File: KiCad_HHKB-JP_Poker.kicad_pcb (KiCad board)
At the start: 2 copper layers, 285 x 95.1 mm, 158 parts, among them SW1 SW_Push, U1 ATmega32U4-MU, U2 PRTR5V0U2X, Y1 16MHz

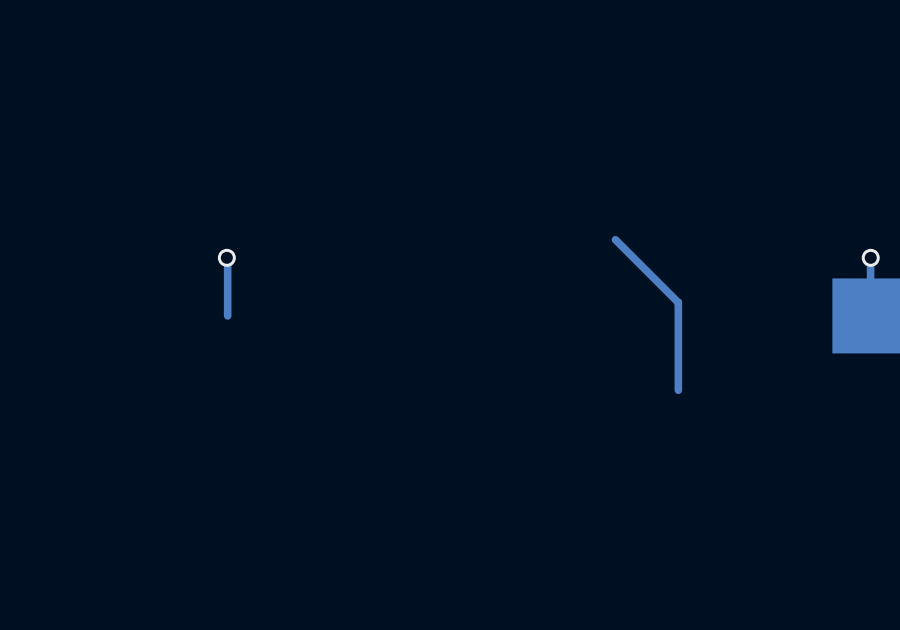
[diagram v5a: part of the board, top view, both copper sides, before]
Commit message: B.Cuの消し残しを削除
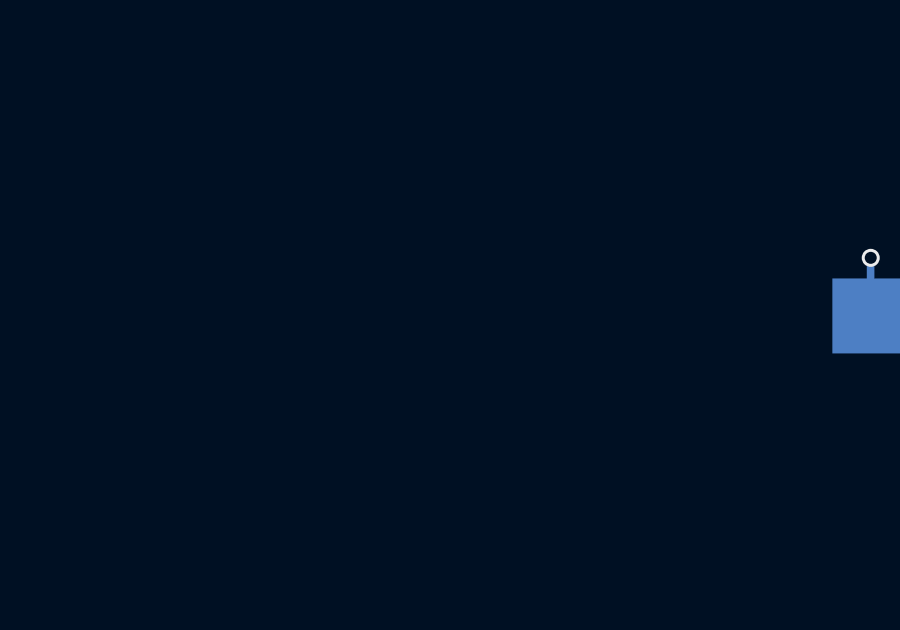
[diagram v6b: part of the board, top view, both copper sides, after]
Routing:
- net Net-(D10-Pad2): track 5.89 -> 0.00 mm
- net COL10: track 67.9 -> 65.9 mm, vias 5 -> 4
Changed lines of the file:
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@@
   (via (at 326.39 200.279) (size 0.6) (drill 0.4) (layers "F.Cu" "B.Cu") (net 79))
   (via (at 341.376 238.379) (size 0.6) (drill 0.4) (layers "F.Cu" "B.Cu") (net 79))
-  (via (at 329.438 253.492) (size 0.6) (drill 0.4) (layers "F.Cu" "B.Cu") (net 79))
   (via (at 331.851 219.329) (size 0.6) (drill 0.4) (layers "F.Cu" "B.Cu") (net 79))
   (segment (start 331.851 219.329) (end 331.851 217.3335) (width 0.254) (layer "B.Cu") (net 79))
   (segment (start 196.6085 311.016) (end 201.80375 311.016) (width 0.254) (layer "B.Cu") (net 79))
   (segment (start 326.39 200.279) (end 326.39 198.9725) (width 0.254) (layer "B.Cu") (net 79))
-  (segment (start 329.438 253.492) (end 329.465 253.519) (width 0.254) (layer "B.Cu") (net 79))
   (segment (start 202.781 307.37175) (end 205.829 304.32375) (width 0.254) (layer "B.Cu") (net 79))
   (segment (start 317.55875 181.17025) (end 317.5 181.229) (width 0.254) (layer "B.Cu") (net 79))
   (segment (start 341.376 236.3835) (end 341.37125 236.37875) (width 0.254) (layer "B.Cu") (net 79))
   (segment (start 201.80375 311.016) (end 202.781 310.03875) (width 0.254) (layer "B.Cu") (net 79))
-  (segment (start 329.465 253.519) (end 329.465 255.42875) (width 0.254) (layer "B.Cu") (net 79))
   (segment (start 317.55875 179.22875) (end 317.55875 181.17025) (width 0.254) (layer "B.Cu") (net 79))
   (segment (start 341.376 238.379) (end 341.376 236.3835) (width 0.254) (layer "B.Cu") (net 79))
@@
   (segment (start 206.375 254.98425) (end 204.2795 252.88875) (width 0.254) (layer "B.Cu") (net 96))
   (segment (start 206.375 257.90625) (end 206.375 254.98425) (width 0.254) (layer "B.Cu") (net 96))
-  (segment (start 344.4875 257.90625) (end 344.4875 254.98425) (width 0.254) (layer "B.Cu") (net 97))
-  (segment (start 344.4875 254.98425) (end 342.392 252.88875) (width 0.254) (layer "B.Cu") (net 97))
   (segment (start 144.653 189.103) (end 141.986 189.103) (width 0.381) (layer "F.Cu") (net 98))
   (segment (start 145.923 181.864) (end 142.24 181.864) (width 0.381) (layer "F.Cu") (net 98))

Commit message: RIGHT の Footprint を 1.25 -> 1U に変更
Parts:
- K_RIGHT1: footprint MX_Only:MXOnly-1.25U-Hotswap -> MX_Only:MXOnly-1U-Hotswap
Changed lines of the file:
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@@
     )
   )
-  (footprint "MX_Only:MXOnly-1.25U-Hotswap" (layer "F.Cu")
+  (footprint "MX_Only:MXOnly-1U-Hotswap" (layer "F.Cu")
     (at 398.4625 257.96875)
     (property "Sheetfile" "matrix.kicad_sch")
     (property "Sheetname" "matrix")
     (attr smd)
-    (fp_text reference "K_RIGHT1" (at 0 3.048) (layer "B.Fab")
+    (fp_text reference "K_RIGHT1" (at 0 3.175) (layer "B.Fab")
       (effects (font (size 1 1) (thickness 0.15)) (justify mirror))
     )
@@
       (effects (font (size 1 1) (thickness 0.15)))
     )
+    (fp_line (start -9.525 9.525) (end -9.525 -9.525) (layer "Dwgs.User") (width 0.15))
+    (fp_line (start 7 -7) (end 7 -5) (layer "Dwgs.User") (width 0.15))
+    (fp_line (start 9.525 -9.525) (end 9.525 9.525) (layer "Dwgs.User") (width 0.15))
     (fp_line (start 7 7) (end 7 5) (layer "Dwgs.User") (width 0.15))
-    (fp_line (start -11.90625 9.525) (end -11.90625 -9.525) (layer "Dwgs.User") (width 0.15))
+    (fp_line (start -7 5) (end -7 7) (layer "Dwgs.User") (width 0.15))
+    (fp_line (start -7 -7) (end -7 -5) (layer "Dwgs.User") (width 0.15))
+    (fp_line (start -5 -7) (end -7 -7) (layer "Dwgs.User") (width 0.15))
+    (fp_line (start 5 7) (end 7 7) (layer "Dwgs.User") (width 0.15))
+    (fp_line (start 9.525 9.525) (end -9.525 9.525) (layer "Dwgs.User") (width 0.15))
+    (fp_line (start -9.525 -9.525) (end 9.525 -9.525) (layer "Dwgs.User") (width 0.15))
+    (fp_line (start 5 -7) (end 7 -7) (layer "Dwgs.User") (width 0.15))
     (fp_line (start -7 7) (end -5 7) (layer "Dwgs.User") (width 0.15))
-    (fp_line (start 5 7) (end 7 7) (layer "Dwgs.User") (width 0.15))
-    (fp_line (start -7 -7) (end -7 -5) (layer "Dwgs.User") (width 0.15))
-    (fp_line (start 11.90625 9.525) (end -11.90625 9.525) (layer "Dwgs.User") (width 0.15))
-    (fp_line (start 7 -7) (end 7 -5) (layer "Dwgs.User") (width 0.15))
-    (fp_line (start -5 -7) (end -7 -7) (layer "Dwgs.User") (width 0.15))
-    (fp_line (start -7 5) (end -7 7) (layer "Dwgs.User") (width 0.15))
-    (fp_line (start -11.90625 -9.525) (end 11.90625 -9.525) (layer "Dwgs.User") (width 0.15))
-    (fp_line (start 5 -7) (end 7 -7) (layer "Dwgs.User") (width 0.15))
-    (fp_line (start 11.90625 -9.525) (end 11.90625 9.525) (layer "Dwgs.User") (width 0.15))
+    (fp_line (start -0.4 -2.6) (end 5.3 -2.6) (layer "B.CrtYd") (width 0.127))
+    (fp_line (start -5.842 -1.27) (end -5.842 -3.81) (layer "B.CrtYd") (width 0.15))
+    (fp_line (start 7.112 -3.81) (end 4.572 -3.81) (layer "B.CrtYd") (width 0.15))
+    (fp_line (start -6.5 -0.6) (end -2.4 -0.6) (layer "B.CrtYd") (width 0.127))
+    (fp_line (start 5.3 -7) (end 5.3 -2.6) (layer "B.CrtYd") (width 0.127))
+    (fp_line (start 4.572 -3.81) (end 4.572 -6.35) (layer "B.CrtYd") (width 0.15))
+    (fp_line (start -6.5 -4.5) (end -6.5 -0.6) (layer "B.CrtYd") (width 0.127))
+    (fp_line (start 5.3 -7) (end -4 -7) (layer "B.CrtYd") (width 0.127))
     (fp_line (start 4.572 -6.35) (end 7.112 -6.35) (layer "B.CrtYd") (width 0.15))
-    (fp_line (start 4.572 -3.81) (end 4.572 -6.35) (layer "B.CrtYd") (width 0.15))
-    (fp_line (start -6.5 -0.6) (end -2.4 -0.6) (layer "B.CrtYd") (width 0.127))
+    (fp_line (start -8.382 -3.81) (end -8.382 -1.27) (layer "B.CrtYd") (width 0.15))
     (fp_line (start 7.112 -6.35) (end 7.112 -3.81) (layer "B.CrtYd") (width 0.15))
-    (fp_line (start 7.112 -3.81) (end 4.572 -3.81) (layer "B.CrtYd") (width 0.15))
-    (fp_line (start 5.3 -7) (end -4 -7) (layer "B.CrtYd") (width 0.127))
-    (fp_line (start -6.5 -4.5) (end -6.5 -0.6) (layer "B.CrtYd") (width 0.127))
-    (fp_line (start 5.3 -7) (end 5.3 -2.6) (layer "B.CrtYd") (width 0.127))
-    (fp_line (start -8.382 -1.27) (end -8.382 -3.81) (layer "B.CrtYd") (width 0.15))
-    (fp_line (start -0.4 -2.6) (end 5.3 -2.6) (layer "B.CrtYd") (width 0.127))
-    (fp_line (start -5.842 -1.27) (end -8.382 -1.27) (layer "B.CrtYd") (width 0.15))
-    (fp_line (start -5.842 -3.81) (end -5.842 -1.27) (layer "B.CrtYd") (width 0.15))
-    (fp_line (start -8.382 -3.81) (end -5.842 -3.81) (layer "B.CrtYd") (width 0.15))
+    (fp_line (start -5.842 -3.81) (end -8.382 -3.81) (layer "B.CrtYd") (width 0.15))
+    (fp_line (start -8.382 -1.27) (end -5.842 -1.27) (layer "B.CrtYd") (width 0.15))
     (fp_arc (start -2.4 -0.6) (mid -1.814214 -2.014214) (end -0.4 -2.6) (layer "B.CrtYd") (width 0.127))
     (fp_arc (start -6.5 -4.5) (mid -5.767767 -6.267767) (end -4 -7) (layer "B.CrtYd") (width 0.127))
+    (fp_circle (center 2.54 -5.08) (end 2.54 -6.604) (layer "B.CrtYd") (width 0.15) (fill none))
     (fp_circle (center -3.81 -2.54) (end -3.81 -4.064) (layer "B.CrtYd") (width 0.15) (fill none))
-    (fp_circle (center 2.54 -5.08) (end 2.54 -6.604) (layer "B.CrtYd") (width 0.15) (fill none))
+    (pad "" np_thru_hole circle locked (at 5.08 0 48.0996) (size 1.75 1.75) (drill 1.75) (layers *.Cu *.Mask))
+    (pad "" np_thru_hole circle locked (at 2.54 -5.08) (size 3 3) (drill 3) (layers *.Cu *.Mask))
+    (pad "" np_thru_hole circle locked (at 0 0) (size 3.9878 3.9878) (drill 3.9878) (layers *.Cu *.Mask))
     (pad "" np_thru_hole circle locked (at -3.81 -2.54) (size 3 3) (drill 3) (layers *.Cu *.Mask))
     (pad "" np_thru_hole circle locked (at -5.08 0 48.0996) (size 1.75 1.75) (drill 1.75) (layers *.Cu *.Mask))
-    (pad "" np_thru_hole circle locked (at 5.08 0 48.0996) (size 1.75 1.75) (drill 1.75) (layers *.Cu *.Mask))
-    (pad "" np_thru_hole circle locked (at 0 0) (size 3.9878 3.9878) (drill 3.9878) (layers *.Cu *.Mask))
-    (pad "" np_thru_hole circle locked (at 2.54 -5.08) (size 3 3) (drill 3) (layers *.Cu *.Mask))
     (pad "1" smd rect locked (at -7.085 -2.54) (size 2.55 2.5) (layers "B.Cu" "B.Paste" "B.Mask")
       (net 82 "COL13") (pinfunction "COL") (pintype "passive"))
@@
     (model "${KILIB}/MX_Alps_Hybrid.pretty/MX_Only.pretty/3d_shapes/CPG151101S11.wrl"
       (offset (xyz 0 0 -1.4868))
-      (scale (xyz 0.3937 0.3937 0.3937))
+      (scale (xyz 0.393701 0.3937 0.393701))
       (rotate (xyz 0 0 0))
     )

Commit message: R4(zxc列)のキースイッチ配置完了
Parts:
- D10, D11, D37, D42, D43: moved to B.Cu
- moved K_UP1 120.7 mm to (381.8, 238.9)
- moved D11 34.3 mm to (324.1, 303.4), turned to 180 degrees
- moved D42 34.3 mm to (324.1, 306.8), turned to 180 degrees
- moved D37 23.4 mm to (318.4, 303.4), turned to 180 degrees
- moved D43 21.0 mm to (331.9, 295.4), turned to 180 degrees
- moved D67 15.6 mm to (393.8, 243.9)
- moved K_RSFT1 7.14 mm to (400.8, 238.9)
- moved D22 4.76 mm to (370.7, 240.5)
- moved D41 4.76 mm to (275.4, 240.5)
- moved K_N1 4.76 mm to (267.5, 238.9)
- moved K_UNSC1 4.76 mm to (362.7, 238.9)
- moved D15 4.76 mm to (183.4, 241.3)
- moved D21 4.76 mm to (199.2, 240.5)
- moved K_B1 4.76 mm to (248.4, 238.9)
- moved K_X1 4.76 mm to (191.3, 238.9)
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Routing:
- net Net-(D67-Pad2): track 6.22 -> 1.17 mm
- net COL13: track 104.4 -> 99.9 mm, vias 5 -> 4
